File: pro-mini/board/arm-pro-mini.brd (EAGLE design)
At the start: 38.1 x 20.3 mm, 57 parts, among them J1 USB, J2 SWD HEADER, Q1 12Mhz, T1 DTA114EET1G (2 X 10K), U1 MCP1754ST-3302E/CB, U2 NUF2042XV6T1G, U3 LPC11U35FHI33/501

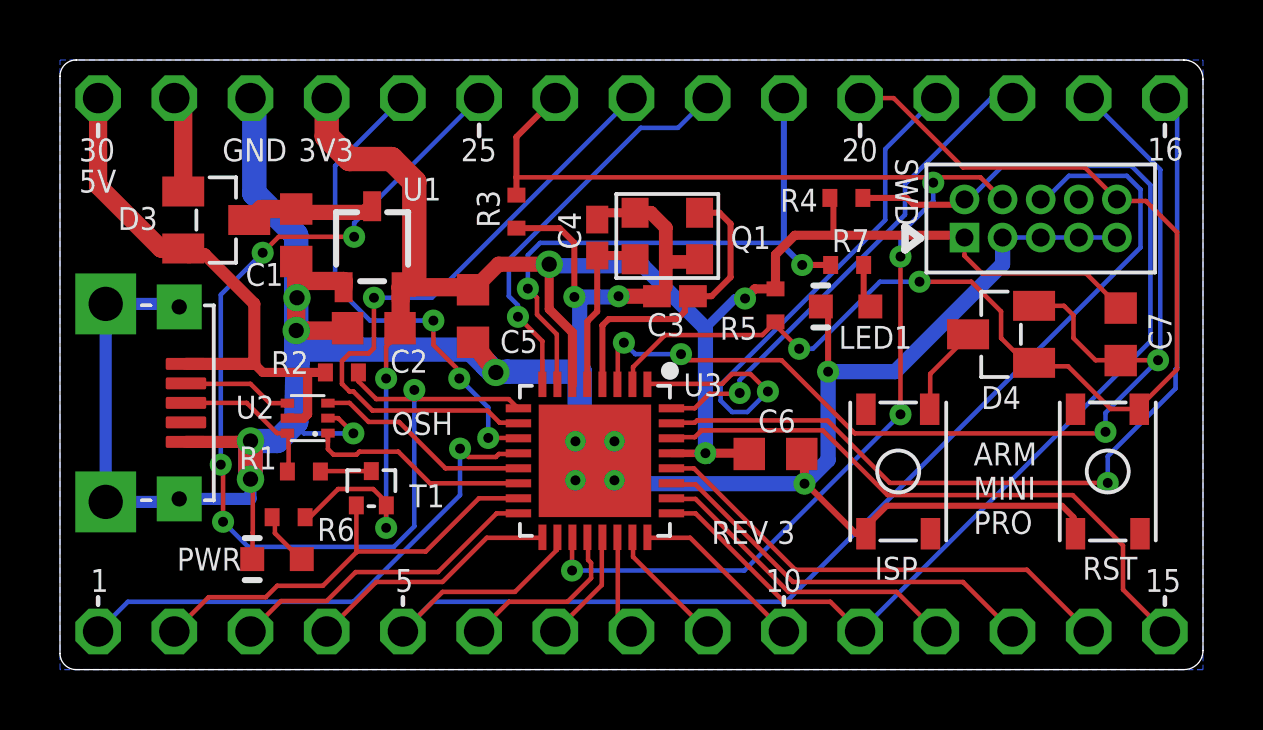
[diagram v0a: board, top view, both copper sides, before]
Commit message: Added vias to switch pads for added mechanicam support. Removed the solder stop of the 4 vias under the MCU. No electrical or stencil change.
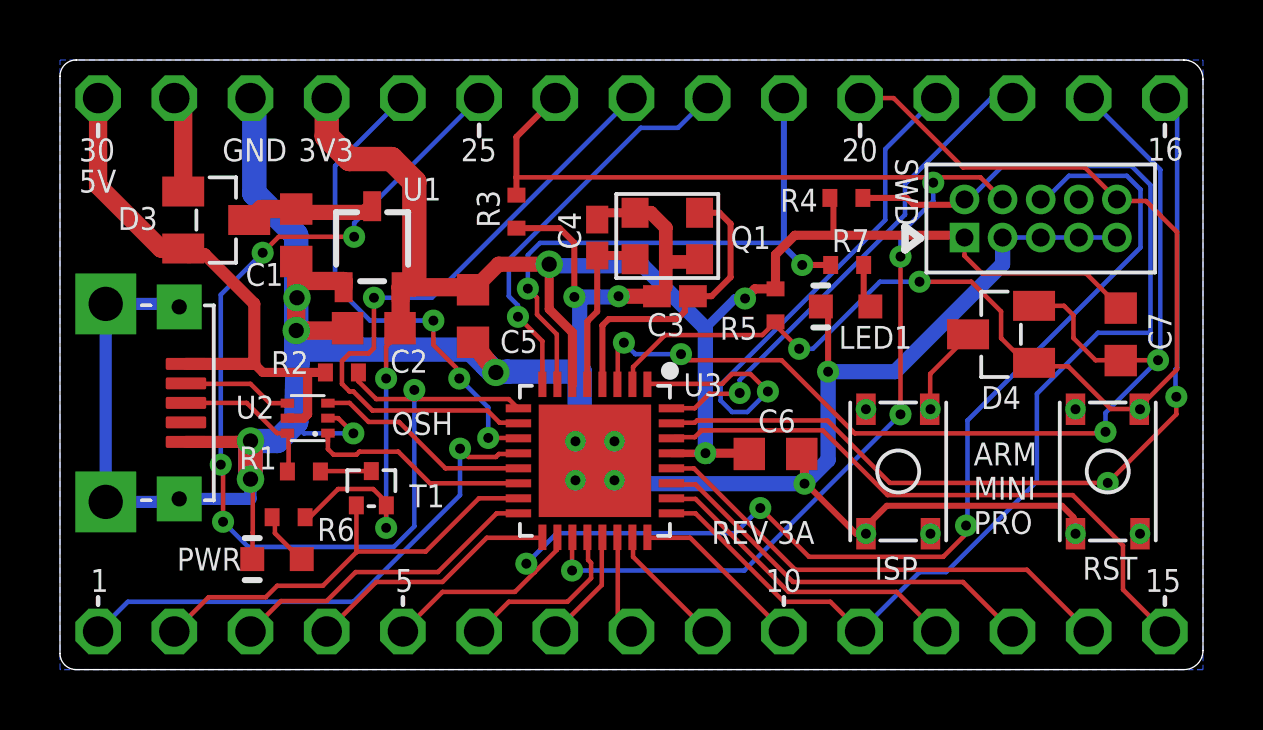
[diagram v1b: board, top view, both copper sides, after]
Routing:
- net PIO0_15-SWDIO: track 37.3 -> 39.1 mm
- net PIO0_9-SWDO: track 42.4 -> 41.2 mm, vias 0 -> 3
- net PIO0_18: vias 1 -> 2
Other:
- board text added: "REV 3A"
- board text removed: "REV 3"
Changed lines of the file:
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@@
 MINI
 PRO</text>
-<text x="21.717" y="4.191" size="0.762" layer="21" font="vector" ratio="10">REV 3</text>
+<text x="21.717" y="4.191" size="0.762" layer="21" font="vector" ratio="10">REV 3A</text>
 <wire x1="1.27" y1="2.413" x2="1.27" y2="2.159" width="0.1524" layer="21"/>
 <wire x1="11.43" y1="2.413" x2="11.43" y2="2.159" width="0.1524" layer="21"/>
@@
 <wire x1="21.2344" y1="8.3058" x2="21.1582" y2="8.2296" width="0.1524" layer="1"/>
 <via x="34.925" y="6.223" extent="1-16" drill="0.3302"/>
-<wire x1="34.925" y1="7.112" x2="34.925" y2="6.223" width="0.1524" layer="16"/>
-<wire x1="37.1856" y1="9.3726" x2="34.925" y2="7.112" width="0.1524" layer="16"/>
 <wire x1="37.1856" y1="10.0076" x2="37.1856" y2="9.3726" width="0.1524" layer="16"/>
 <wire x1="37.1856" y1="10.0076" x2="37.2364" y2="10.0584" width="0.1524" layer="16"/>
 <wire x1="27.6606" y1="6.223" x2="34.925" y2="6.223" width="0.1524" layer="1"/>
+<wire x1="37.211" y1="9.0932" x2="37.211" y2="9.3218" width="0.1524" layer="16"/>
+<wire x1="37.211" y1="8.509" x2="37.211" y2="9.0932" width="0.1524" layer="1"/>
+<wire x1="34.925" y1="6.223" x2="37.211" y2="8.509" width="0.1524" layer="1"/>
+<wire x1="37.211" y1="9.3218" x2="37.1856" y2="9.3726" width="0.1524" layer="16"/>
+<via x="37.211" y="9.0932" extent="1-16" drill="0.3302"/>
 </signal>
 <signal name="PIO0_19">
@@
 <via x="17.0688" y="3.302" extent="1-16" drill="0.3302"/>
 <wire x1="29.1084" y1="16.4084" x2="15.2146" y2="16.4084" width="0.1524" layer="1"/>
-<wire x1="28.0162" y1="8.509" x2="22.8092" y2="3.302" width="0.1524" layer="16"/>
-<wire x1="28.0162" y1="13.7668" x2="28.0162" y2="8.509" width="0.1524" layer="1"/>
 <wire x1="28.0162" y1="14.5288" x2="28.0162" y2="13.7668" width="0.1524" layer="16"/>
 <wire x1="29.1084" y1="15.621" x2="28.0162" y2="14.5288" width="0.1524" layer="16"/>
 <wire x1="29.1084" y1="16.2306" x2="29.1084" y2="15.621" width="0.1524" layer="16"/>
 <wire x1="29.1084" y1="16.4084" x2="29.1084" y2="16.2306" width="0.1524" layer="1"/>
-<via x="28.0162" y="8.509" extent="1-16" drill="0.3302"/>
 <via x="28.0162" y="13.7668" extent="1-16" drill="0.3302"/>
 <via x="29.1084" y="16.2306" extent="1-16" drill="0.3302"/>
+<wire x1="28.0162" y1="8.509" x2="22.8092" y2="3.302" width="0.1524" layer="16"/>
+<wire x1="28.0162" y1="13.7668" x2="28.0162" y2="8.509" width="0.1524" layer="1"/>
+<via x="28.0162" y="8.509" extent="1-16" drill="0.3302"/>
 </signal>
 <signal name="PIO0_15-SWDIO">
@@
 <wire x1="35.7124" y1="16.7894" x2="31.4198" y2="16.7894" width="0.1524" layer="16"/>
 <wire x1="36.3474" y1="16.1544" x2="35.7124" y2="16.7894" width="0.1524" layer="16"/>
-<wire x1="26.67" y1="1.27" x2="36.3474" y2="10.9474" width="0.1524" layer="16"/>
-<wire x1="36.3474" y1="10.9474" x2="36.3474" y2="16.1544" width="0.1524" layer="16"/>
+<wire x1="36.3474" y1="10.9474" x2="36.3474" y2="11.2268" width="0.1524" layer="16"/>
+<wire x1="36.3474" y1="11.2268" x2="36.3474" y2="16.1544" width="0.1524" layer="16"/>
 <wire x1="30.0736" y1="15.5956" x2="29.972" y2="15.494" width="0.2032" layer="1"/>
 <wire x1="29.972" y1="15.494" x2="28.448" y2="15.494" width="0.2032" layer="1"/>
 <wire x1="28.448" y1="15.494" x2="28.2194" y2="15.7226" width="0.2032" layer="1"/>
 <wire x1="28.2194" y1="15.7226" x2="26.7628" y2="15.7226" width="0.2032" layer="1"/>
+<wire x1="28.6512" y1="3.2512" x2="26.67" y2="1.27" width="0.1524" layer="16"/>
+<wire x1="29.5402" y1="3.2512" x2="28.6512" y2="3.2512" width="0.1524" layer="16"/>
+<wire x1="32.5628" y1="6.2738" x2="29.5402" y2="3.2512" width="0.1524" layer="16"/>
+<wire x1="32.5628" y1="9.1948" x2="32.5628" y2="6.2738" width="0.1524" layer="16"/>
+<wire x1="34.5948" y1="11.2268" x2="32.5628" y2="9.1948" width="0.1524" layer="16"/>
+<wire x1="36.3474" y1="11.2268" x2="34.5948" y2="11.2268" width="0.1524" layer="16"/>
 </signal>
 <signal name="PIO0_1-ISP_EN">
@@
 <contactref element="TP5" pad="1"/>
 <wire x1="16.5608" y1="3.9878" x2="16.5608" y2="4.3942" width="0.1524" layer="1"/>
-<wire x1="15.1638" y1="2.5908" x2="16.5608" y2="3.9878" width="0.1524" layer="1"/>
+<wire x1="15.1638" y1="2.5908" x2="15.8242" y2="3.2512" width="0.1524" layer="1"/>
+<wire x1="15.8242" y1="3.2512" x2="16.5608" y2="3.9878" width="0.1524" layer="1"/>
 <wire x1="12.7508" y1="2.5908" x2="15.1638" y2="2.5908" width="0.1524" layer="1"/>
 <wire x1="11.43" y1="1.27" x2="12.7508" y2="2.5908" width="0.1524" layer="1"/>
@@
 <wire x1="36.0172" y1="16.002" x2="35.56" y2="16.4592" width="0.1524" layer="16"/>
 <wire x1="36.0172" y1="14.0716" x2="36.0172" y2="16.002" width="0.1524" layer="16"/>
-<wire x1="24.2062" y1="2.2606" x2="36.0172" y2="14.0716" width="0.1524" layer="16"/>
-<wire x1="12.4206" y1="2.2606" x2="24.2062" y2="2.2606" width="0.1524" layer="16"/>
-<wire x1="11.43" y1="1.27" x2="12.4206" y2="2.2606" width="0.1524" layer="16"/>
+<wire x1="30.2514" y1="8.3058" x2="36.0172" y2="14.0716" width="0.1524" layer="16"/>
+<wire x1="30.2514" y1="4.8514" x2="30.2514" y2="8.3058" width="0.1524" layer="16"/>
+<wire x1="30.2006" y1="4.8006" x2="30.2514" y2="4.8514" width="0.1524" layer="16"/>
+<wire x1="30.2006" y1="4.5212" x2="30.2006" y2="4.8006" width="0.1524" layer="1"/>
+<wire x1="29.4386" y1="3.7592" x2="30.2006" y2="4.5212" width="0.1524" layer="1"/>
+<wire x1="24.9682" y1="3.7592" x2="29.4386" y2="3.7592" width="0.1524" layer="1"/>
+<wire x1="23.3426" y1="5.3848" x2="24.9682" y2="3.7592" width="0.1524" layer="1"/>
+<wire x1="22.5044" y1="4.5466" x2="23.3426" y2="5.3848" width="0.1524" layer="16"/>
+<wire x1="16.5608" y1="4.5466" x2="22.5044" y2="4.5466" width="0.1524" layer="16"/>
+<wire x1="15.5448" y1="3.5306" x2="16.5608" y2="4.5466" width="0.1524" layer="16"/>
+<wire x1="15.8242" y1="3.2512" x2="15.5448" y2="3.5306" width="0.1524" layer="1"/>
+<via x="30.2006" y="4.8006" extent="1-16" drill="0.3302"/>
+<via x="23.3426" y="5.3848" extent="1-16" drill="0.3302"/>
+<via x="15.5448" y="3.5306" extent="1-16" drill="0.3302"/>
 </signal>
 <signal name="N$4" class="2">

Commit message: Reduced the number of approved layout errors. Added stop layer to the vias on the switches pads. No electrical, placement or stencil change.
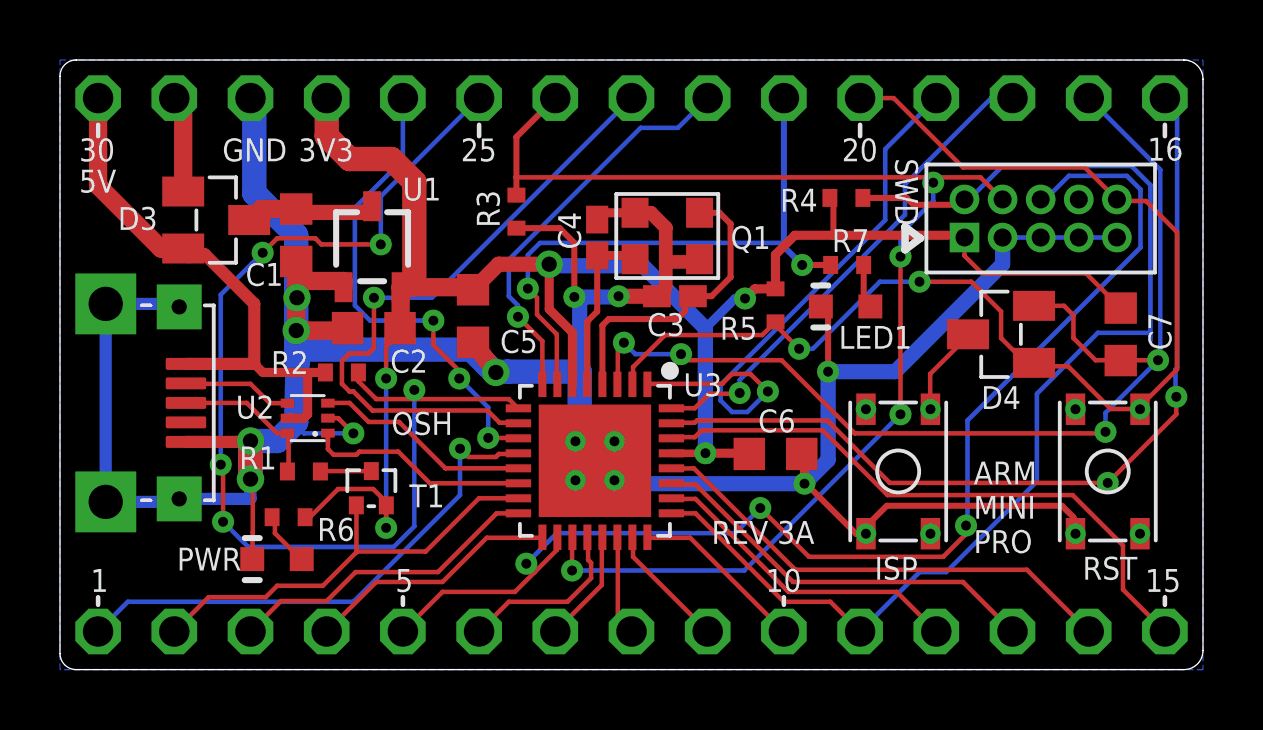
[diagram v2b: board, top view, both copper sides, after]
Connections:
- net GND: now also S1.A1P, S2.A1P
- net N$8: now also S1.B2P
- net PIO0_0-RESET: now also S2.B2P
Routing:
- net PIO0_3-VBUS: track 37.1 -> 37.9 mm
- net PIO0_5: track 16.6 -> 16.1 mm
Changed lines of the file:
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@@
 <text x="0.635" y="16.9418" size="0.762" layer="21" font="vector" ratio="10">30</text>
 <text x="27.8384" y="17.0434" size="0.762" layer="21" font="vector" ratio="10" rot="SR270">SWD</text>
-<text x="30.4546" y="4.5212" size="0.762" layer="21" font="vector" ratio="10">ARM
+<text x="30.4546" y="3.8862" size="0.762" layer="21" font="vector" ratio="10">ARM
 MINI
 PRO</text>
@@
 <wire x1="24.8158" y1="6.1976" x2="25.6032" y2="6.985" width="0.508" layer="16"/>
 <wire x1="25.6032" y1="6.985" x2="25.6032" y2="9.9314" width="0.508" layer="16"/>
+<contactref element="S1" pad="A1P"/>
+<contactref element="S2" pad="A1P"/>
 </signal>
 <signal name="N$1">
@@
 <wire x1="12.446" y1="11.6332" x2="12.446" y2="10.8204" width="0.1524" layer="1"/>
 <wire x1="10.3378" y1="11.6332" x2="12.446" y2="11.6332" width="0.1524" layer="16"/>
-<wire x1="9.1694" y1="12.8016" x2="10.3378" y2="11.6332" width="0.1524" layer="16"/>
-<wire x1="9.1694" y1="16.7894" x2="9.1694" y2="12.8016" width="0.1524" layer="16"/>
-<wire x1="11.43" y1="19.05" x2="9.1694" y2="16.7894" width="0.1524" layer="16"/>
 <wire x1="15.1892" y1="7.7216" x2="15.2808" y2="7.7096" width="0.1524" layer="1"/>
 <via x="14.2748" y="7.7216" extent="1-16" drill="0.3302"/>
 <via x="13.3096" y="9.7028" extent="1-16" drill="0.3302"/>
 <via x="12.446" y="11.6332" extent="1-16" drill="0.3302"/>
+<wire x1="11.43" y1="16.9926" x2="11.43" y2="19.05" width="0.1524" layer="16"/>
+<wire x1="9.8298" y1="15.3924" x2="11.43" y2="16.9926" width="0.1524" layer="16"/>
+<wire x1="9.8298" y1="12.1412" x2="9.8298" y2="15.3924" width="0.1524" layer="16"/>
+<wire x1="10.3378" y1="11.6332" x2="9.8298" y2="12.1412" width="0.1524" layer="16"/>
 </signal>
 <signal name="PIO0_6-CONNECT">
@@
 <wire x1="5.3594" y1="12.4968" x2="5.3594" y2="6.8326" width="0.1524" layer="16"/>
 <wire x1="6.7564" y1="13.8938" x2="5.3594" y2="12.4968" width="0.1524" layer="16"/>
-<wire x1="7.2898" y1="14.4272" x2="6.7564" y2="13.8938" width="0.1524" layer="1"/>
-<wire x1="9.8044" y1="14.4272" x2="7.2898" y2="14.4272" width="0.1524" layer="1"/>
-<wire x1="9.8044" y1="14.8844" x2="9.8044" y2="14.4272" width="0.1524" layer="16"/>
-<wire x1="13.97" y1="19.05" x2="9.8044" y2="14.8844" width="0.1524" layer="16"/>
 <via x="11.811" y="9.3218" extent="1-16" drill="0.3302"/>
 <via x="5.4356" y="4.9276" extent="1-16" drill="0.3302"/>
 <via x="5.3594" y="6.8326" extent="1-16" drill="0.3302"/>
 <via x="6.7564" y="13.8938" extent="1-16" drill="0.3302"/>
-<via x="9.8044" y="14.4272" extent="1-16" drill="0.3302"/>
+<via x="10.6934" y="14.1732" extent="1-16" drill="0.3302"/>
 <wire x1="10.541" y1="9.017" x2="9.948" y2="9.61" width="0.1524" layer="1"/>
 <wire x1="9.948" y1="9.61" x2="9.948" y2="9.906" width="0.1524" layer="1"/>
+<wire x1="10.6934" y1="15.7734" x2="10.6934" y2="14.1732" width="0.1524" layer="16"/>
+<wire x1="13.97" y1="19.05" x2="10.6934" y2="15.7734" width="0.1524" layer="16"/>
+<wire x1="8.7122" y1="14.1732" x2="10.6934" y2="14.1732" width="0.1524" layer="1"/>
+<wire x1="8.509" y1="14.3764" x2="8.7122" y2="14.1732" width="0.1524" layer="1"/>
+<wire x1="7.239" y1="14.3764" x2="8.509" y2="14.3764" width="0.1524" layer="1"/>
+<wire x1="6.7564" y1="13.8938" x2="7.239" y2="14.3764" width="0.1524" layer="1"/>
 </signal>
 <signal name="USB-5V">
@@
 <wire x1="33.6042" y1="10.1092" x2="35.0266" y2="8.6868" width="0.1524" layer="1"/>
 <wire x1="32.5374" y1="10.1092" x2="33.6042" y2="10.1092" width="0.1524" layer="1"/>
-<wire x1="35.9664" y1="8.6868" x2="35.975" y2="8.679" width="0.1524" layer="1"/>
+<wire x1="35.9664" y1="8.6868" x2="36" y2="8.679" width="0.1524" layer="1"/>
 <wire x1="32.5374" y1="10.1092" x2="32.469" y2="10.226" width="0.1524" layer="1"/>
 <wire x1="37.2364" y1="10.0076" x2="37.2364" y2="14.5796" width="0.1524" layer="1"/>
 <wire x1="35.9918" y1="8.763" x2="37.2364" y2="10.0076" width="0.1524" layer="1"/>
-<wire x1="35.9918" y1="8.763" x2="35.975" y2="8.679" width="0.1524" layer="1"/>
+<wire x1="35.9918" y1="8.763" x2="36" y2="8.679" width="0.1524" layer="1"/>
 <via x="24.638" y="10.6934" extent="1-16" drill="0.3302"/>
 <via x="28.6512" y="12.9286" extent="1-16" drill="0.3302"/>
@@
 <wire x1="27.3304" y1="12.9286" x2="25.0952" y2="10.6934" width="0.1524" layer="16"/>
 <wire x1="25.0952" y1="10.6934" x2="24.638" y2="10.6934" width="0.1524" layer="16"/>
+<contactref element="S2" pad="B2P"/>
 </signal>
 <signal name="PIO0_10-SWDCLK">
@@
 <wire x1="29.0068" y1="9.8552" x2="29.0068" y2="8.6868" width="0.1524" layer="1"/>
 <wire x1="30.2514" y1="11.0998" x2="29.0068" y2="9.8552" width="0.1524" layer="1"/>
-<wire x1="29.0068" y1="8.6868" x2="28.99" y2="8.679" width="0.1524" layer="1"/>
+<wire x1="29.0068" y1="8.6868" x2="29.015" y2="8.679" width="0.1524" layer="1"/>
 <wire x1="30.2514" y1="11.0998" x2="30.269" y2="11.176" width="0.1524" layer="1"/>
+<contactref element="S1" pad="B2P"/>
 </signal>
 </signals>

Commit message: Minor tweaks, extended pads of the crystial, transistor and USB connector for easier hand soldering. Fixed 'ARM MINI PRO' label to 'ARM PRO MINI'. Most Had to move the crystal a little bit so existing stencils from version 3A may or may not fit this new version 3B.
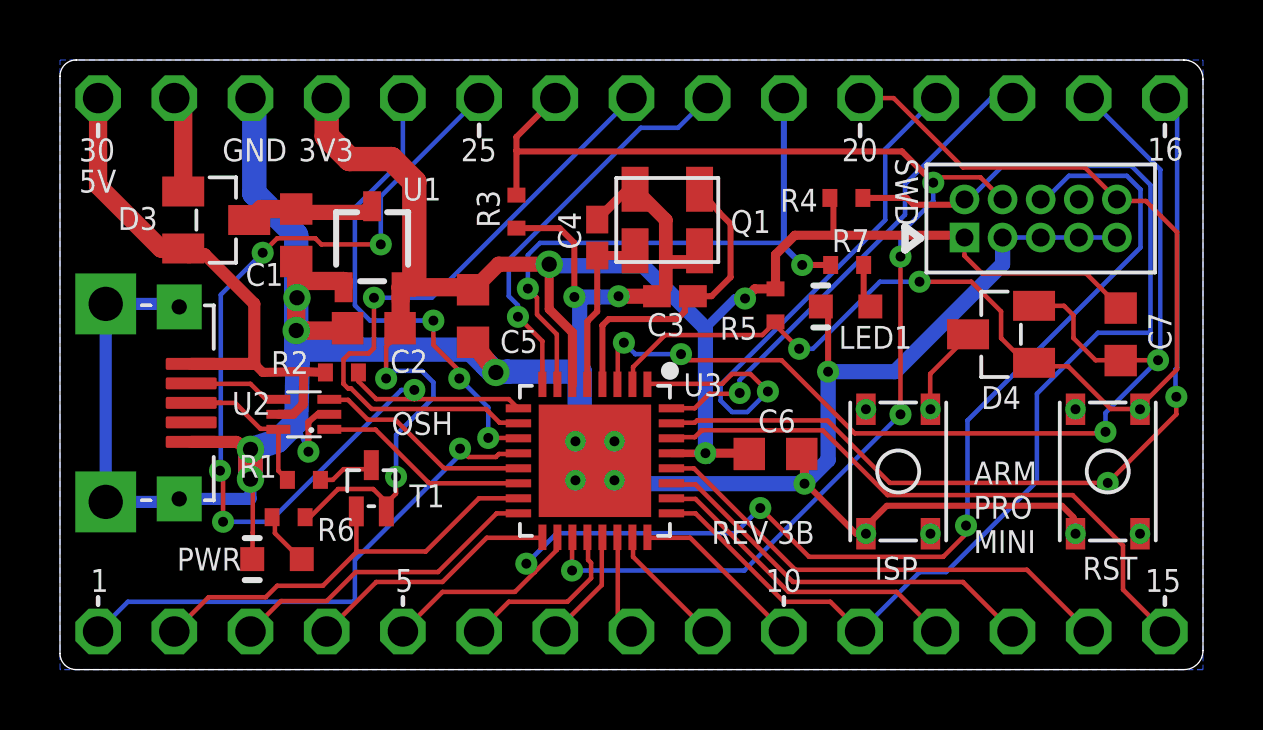
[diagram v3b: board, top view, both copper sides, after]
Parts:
- moved Q1 0.53 mm to (20.2, 15.0)
- moved R1 0.28 mm to (8.13, 6.32)
- moved U2 0.18 mm to (8.13, 8.51)
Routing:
- net PIO0_3-VBUS: track 37.9 -> 35.0 mm
- net +3V3: track 63.9 -> 65.8 mm
- net N$7: track 5.11 -> 6.15 mm
- net USB_DP: track 7.75 -> 7.04 mm
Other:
- board text added: "ARM PRO MINI"
- board text added: "REV 3B"
- board text removed: "ARM MINI PRO"
- board text removed: "REV 3A"
